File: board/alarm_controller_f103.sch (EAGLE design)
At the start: 145 parts, among them IC3 AT24C, U1 STM32F10XRXT6, X1 RJ45-8L21-S, X2 RJ45-8L21-S

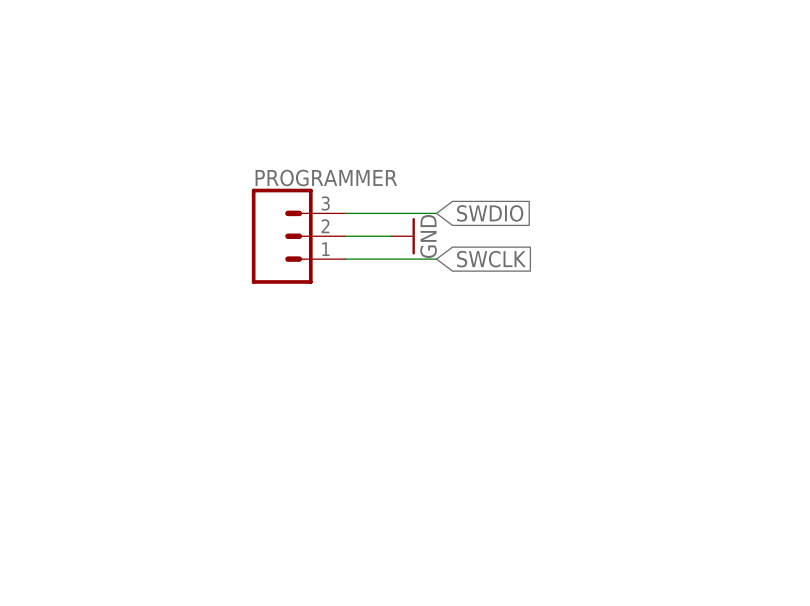
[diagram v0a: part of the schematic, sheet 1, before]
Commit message: add 3.3v to swd connector
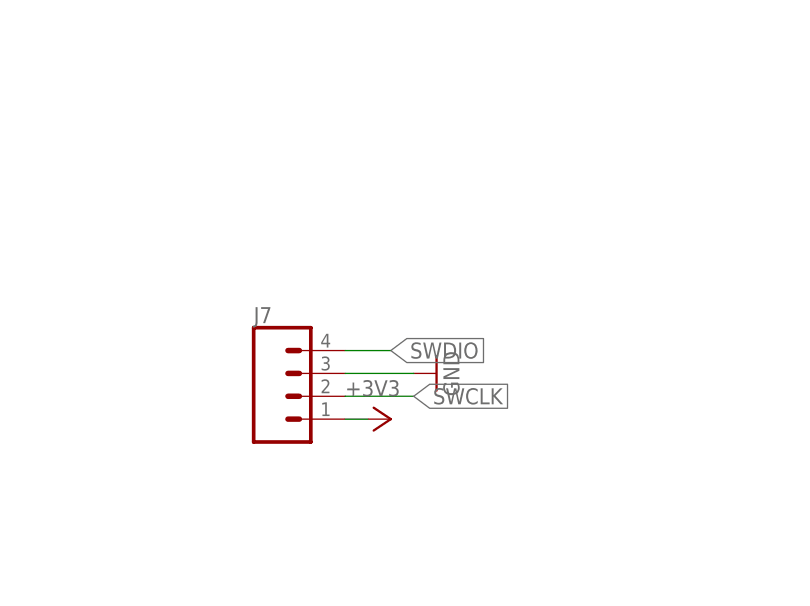
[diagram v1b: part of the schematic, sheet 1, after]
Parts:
- removed PROGRAMMER: (no value), SparkFun-Connectors:CONN_03LOCK
- added J7: (no value), SparkFun-Connectors:CONN_04POLAR_LOCK
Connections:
- net +3V3: now also J7.1
- net GND: now also J7.3; no longer PROGRAMMER.2
- net SWCLK: now also J7.2; no longer PROGRAMMER.1
- net SWDIO: now also J7.4; no longer PROGRAMMER.3
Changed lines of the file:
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@@
 <part name="GND12" library="supply1" deviceset="GND" device=""/>
 <part name="+3V8" library="supply1" deviceset="+3V3" device=""/>
-<part name="PROGRAMMER" library="SparkFun-Connectors" deviceset="CONN_03" device="LOCK"/>
-<part name="GND13" library="supply1" deviceset="GND" device=""/>
 <part name="DA1" library="transceiver" deviceset="SN65HVD232" device=""/>
 <part name="+3V1" library="supply1" deviceset="+3V3" device=""/>
@@
 <part name="C32" library="microbuilder" deviceset="CAP_CERAMIC" device="0603MINI" value="100nf"/>
 <part name="C33" library="microbuilder" deviceset="CAP_CERAMIC" device="0603MINI" value="1uf"/>
+<part name="+3V5" library="supply1" deviceset="+3V3" device=""/>
+<part name="GND1" library="supply1" deviceset="GND" device=""/>
+<part name="J7" library="SparkFun-Connectors" deviceset="CONN_04" device="POLAR_LOCK"/>
 </parts>
 <sheets>
@@
 <instance part="GND12" gate="1" x="22.86" y="-53.34"/>
 <instance part="+3V8" gate="G$1" x="22.86" y="-30.48"/>
-<instance part="PROGRAMMER" gate="J$1" x="-160.02" y="83.82"/>
-<instance part="GND13" gate="1" x="-144.78" y="83.82" rot="R90"/>
 <instance part="DA1" gate="G$1" x="-269.24" y="-48.26"/>
 <instance part="+3V1" gate="G$1" x="-287.02" y="-43.18"/>
@@
 <instance part="C23" gate="G$1" x="30.48" y="-43.18"/>
 <instance part="C27" gate="G$1" x="38.1" y="-43.18"/>
+<instance part="+3V5" gate="G$1" x="-147.32" y="63.5" rot="R270"/>
+<instance part="GND1" gate="1" x="-142.24" y="68.58" rot="R90"/>
+<instance part="J7" gate="G$1" x="-157.48" y="66.04"/>
 </instances>
 <busses>
@@
 </segment>
 <segment>
-<pinref part="PROGRAMMER" gate="J$1" pin="2"/>
-<pinref part="GND13" gate="1" pin="GND"/>
-<wire x1="-147.32" y1="83.82" x2="-152.4" y2="83.82" width="0.1524" layer="91"/>
-</segment>
-<segment>
 <pinref part="R5" gate="G$1" pin="1"/>
 <pinref part="GND4" gate="1" pin="GND"/>
@@
 <wire x1="-218.44" y1="71.12" x2="-215.9" y2="71.12" width="0.1524" layer="91"/>
 <pinref part="GND100" gate="1" pin="GND"/>
+</segment>
+<segment>
+<pinref part="GND1" gate="1" pin="GND"/>
+<wire x1="-144.78" y1="68.58" x2="-152.4" y2="68.58" width="0.1524" layer="91"/>
+<pinref part="J7" gate="G$1" pin="3"/>
 </segment>
 </net>
@@
 <wire x1="-43.18" y1="134.62" x2="-38.1" y2="134.62" width="0.1524" layer="91"/>
 </segment>
+<segment>
+<pinref part="+3V5" gate="G$1" pin="+3V3"/>
+<wire x1="-149.86" y1="63.5" x2="-152.4" y2="63.5" width="0.1524" layer="91"/>
+<pinref part="J7" gate="G$1" pin="1"/>
+</segment>
 </net>
 <net name="+12V" class="0">
@@
 <net name="SWDIO" class="0">
 <segment>
-<pinref part="PROGRAMMER" gate="J$1" pin="3"/>
-<wire x1="-152.4" y1="86.36" x2="-142.24" y2="86.36" width="0.1524" layer="91"/>
-<label x="-142.24" y="86.36" size="1.778" layer="95" xref="yes"/>
+<wire x1="-152.4" y1="71.12" x2="-147.32" y2="71.12" width="0.1524" layer="91"/>
+<label x="-147.32" y="71.12" size="1.778" layer="95" xref="yes"/>
+<pinref part="J7" gate="G$1" pin="4"/>
 </segment>
 </net>
 <net name="SWCLK" class="0">
 <segment>
-<label x="-142.24" y="81.28" size="1.778" layer="95" xref="yes"/>
-<pinref part="PROGRAMMER" gate="J$1" pin="1"/>
-<wire x1="-152.4" y1="81.28" x2="-142.24" y2="81.28" width="0.1524" layer="91"/>
+<wire x1="-152.4" y1="66.04" x2="-144.78" y2="66.04" width="0.1524" layer="91"/>
+<label x="-144.78" y="66.04" size="1.778" layer="95" xref="yes"/>
+<pinref part="J7" gate="G$1" pin="2"/>
 </segment>
 </net>
